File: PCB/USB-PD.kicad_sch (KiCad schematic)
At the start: 62 parts, among them J2 61300411121, Q10 SQJB90EP-T1_GE3, Q11 AO3404A, Q8 AO3404A, Q9 AO3404A, U4 TPS26750SRSMR, U5 LM2765, U6 CAT24C512YI-GT3, U7 74LVC1G08SE-7, U8 LTC7004x

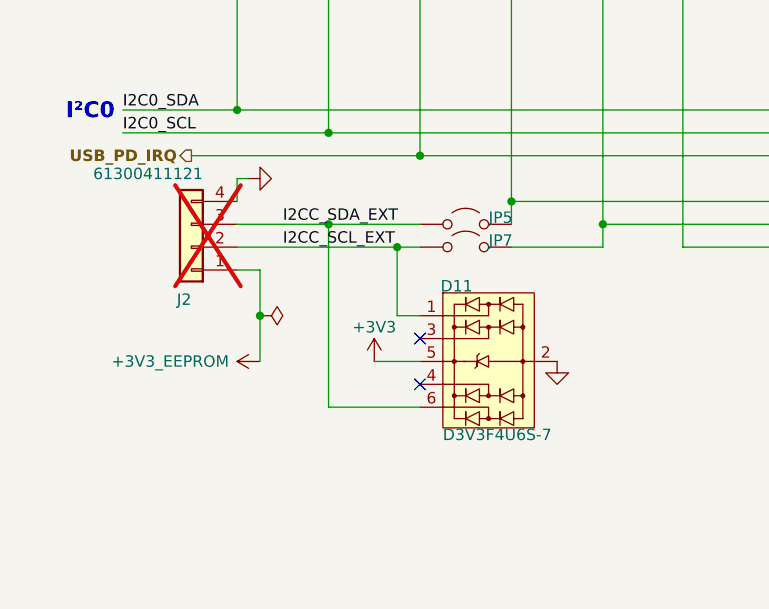
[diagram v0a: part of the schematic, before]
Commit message: Revision 2; gate diodes, 5V into LT, i2c and uart lines fixed
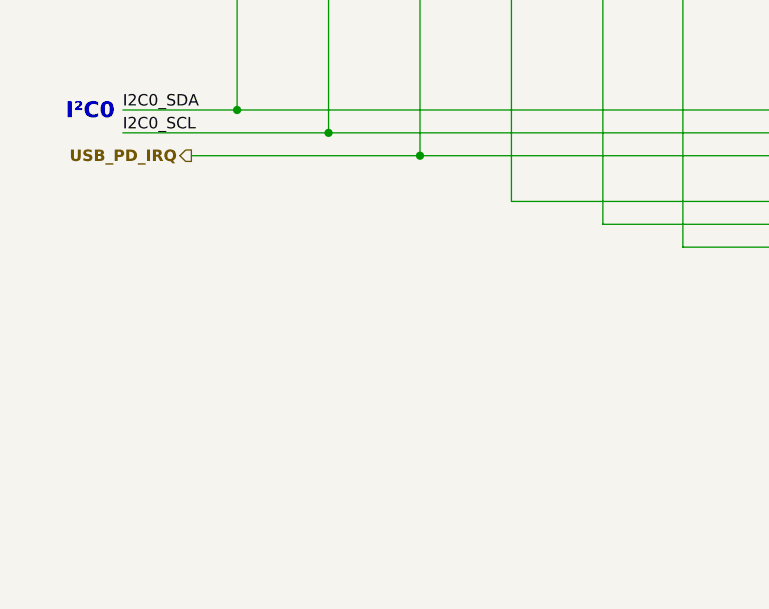
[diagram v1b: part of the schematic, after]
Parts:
- removed D11: D3V3F4U6S-7, Altium_port:sot363_sc88_65p_200x125x110_n, symbol 0_PD240W:D3V3F4U6S-7
- removed J2: 61300411121, Altium_port:we_61300411121, symbol Connector_Generic:Conn_01x04
- removed JP5, JP7: jumper_solder_2pad_no, Altium_port:jumper_solder_2pad_no_40x40_20, symbol Jumper:Jumper_2_Open
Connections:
- no-connect marks 4 -> 2

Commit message: Added NMOS output switch (rated for 20A this time)
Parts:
- removed C50: 100n X7R 100V, Capacitor_SMD:C_0603_1608Metric, symbol 0_passives:C_0603
- removed JP14: Jumper_2_Bridged, Jumper:SolderJumper-2_P1.3mm_Bridged_RoundedPad1.0x1.5mm, symbol Jumper:Jumper_2_Bridged
- removed JP4, JP6, JP8, JP9: jumper_solder_2pad_no, Jumper:SolderJumper-2_P1.3mm_Open_RoundedPad1.0x1.5mm, symbol Jumper:Jumper_2_Open
- removed R37: 100k, Resistor_SMD:R_0402_1005Metric, symbol Device:R_Small
- removed U7: 74LVC1G08SE-7, Altium_port:sot353_65p_200x125x110_mo-203-aa_n, symbol 0_PD240W:74LVC1G08SE-7
- added JP4, JP5: SolderJumper_3_Open, Jumper:SolderJumper-3_P1.3mm_Open_RoundedPad1.0x1.5mm, symbol Jumper:SolderJumper_3_Open
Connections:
- net I2CC_SCL: now also R35.2, JP4.1 (A)
- net I2CC_SCL_EEPROM: now also JP4.2 (C); no longer R35.2
- net I2CC_SCL_MCU: now also JP4.3 (B)
- net I2CC_SDA: now also R34.2, JP5.1 (A)
- net I2CC_SDA_EEPROM: now also JP5.2 (C); no longer R34.2
- net I2CC_SDA_MCU: now also JP5.3 (B)
- net PP_EN2: now also R41.1, R91.2
- net PP_EN3: no longer R41.1, R91.2
- net TS: no longer C51.1, JP11.2 (C)
- new net: C51.1, JP11.2 (C)
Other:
- moved on the sheet: Q8, Q9, R38, R39

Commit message: Preliminary finish of Rev3
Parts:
- removed D13: APTD1608LQBC/D, Altium_port:kingbright_0603_blue, symbol 0_PD240W:APTD1608LQBC/D
- removed Q11: AO3404A, Altium_port:sot-23-3L_103p_300x130x110_n, symbol Transistor_FET_Other:Q_NMOS_Depletion_GSD
- removed R45: 330R 1%, Resistor_SMD:R_0402_1005Metric, symbol 0_passives:R_0402
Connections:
- net SWITCH_EN: no longer names the net of R41.2, U8.4 (INP)

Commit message: Rev3 software now running and working. Couple hardware bugs being fixed for R4
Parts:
- removed R91: 10k, Resistor_SMD:R_0402_1005Metric, symbol Device:R
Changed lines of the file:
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@@
 	)
 	(junction
-		(at 293.37 114.3)
-		(diameter 0)
-		(color 0 0 0 0)
-	)
-	(junction
 		(at 208.28 142.24)
 		(diameter 0)
@@
 		)
 	)
-	(wire
-		(pts
-			(xy 293.37 114.3) (xy 293.37 118.11)
-		)
-		(stroke
-			(width 0)
-			(type default)
-		)
-	)
 	(bus
 		(pts
@@
 	(wire
 		(pts
-			(xy 293.37 125.73) (xy 293.37 129.54)
-		)
-		(stroke
-			(width 0)
-			(type default)
-		)
-	)
-	(wire
-		(pts
 			(xy 71.12 198.12) (xy 54.61 198.12)
 		)
@@
 	(symbol
 		(lib_id "power:GND")
-		(at 293.37 129.54 0)
-		(unit 1)
-		(body_style 1)
-		(exclude_from_sim no)
-		(in_bom yes)
-		(on_board yes)
-		(in_pos_files yes)
-		(dnp no)
-		(property "Reference" "#PWR090"
-			(at 293.37 129.54 0)
-			(hide yes)
-			(show_name no)
-			(do_not_autoplace no)
-			(effects
-				(font
-					(size 1.27 1.27)
-				)
-			)
-		)
-		(property "Value" "GND"
-			(at 293.37 135.89 0)
-			(hide yes)
-			(show_name no)
-			(do_not_autoplace no)
-			(effects
-				(font
-					(size 1.27 1.27)
-				)
-			)
-		)
-		(property "Footprint" ""
-			(at 293.37 129.54 0)
-			(show_name no)
-			(do_not_autoplace no)
-			(effects
-				(font
-					(size 1.27 1.27)
-				)
-			)
-		)
-		(property "Datasheet" ""
-			(at 293.37 129.54 0)
-			(show_name no)
-			(do_not_autoplace no)
-			(effects
-				(font
-					(size 1.27 1.27)
-				)
-			)
-		)
-		(property "Description" ""
-			(at 293.37 129.54 0)
-			(show_name no)
-			(do_not_autoplace no)
-			(effects
-				(font
-					(size 1.27 1.27)
-				)
-			)
-		)
-		(pin "1"
-		)
-		(instances
-			(project "nitride-nano"
-				(path "/aaad0350-e7db-44d5-b7ef-99e6416f6948/a05511eb-3c5e-4a0d-8491-3131eaddecdc"
-					(reference "#PWR090")
-					(unit 1)
-				)
-			)
-		)
-	)
-	(symbol
-		(lib_id "power:GND")
 		(at 143.51 74.93 0)
 		(unit 1)
@@
 					(unit 1)
 				)
-			)
-		)
-	)
-	(symbol
-		(lib_id "Device:R")
-		(at 293.37 121.92 0)
-		(mirror x)
-		(unit 1)
-		(body_style 1)
-		(exclude_from_sim no)
-		(in_bom yes)
-		(on_board yes)
-		(in_pos_files yes)
-		(dnp no)
-		(fields_autoplaced yes)
-		(property "Reference" "R91"
-			(at 295.91 123.1901 0)
-			(show_name no)
-			(do_not_autoplace no)
-			(effects
-				(font
-					(size 1.27 1.27)
-				)
-				(justify left)
-			)
-		)
-		(property "Value" "10k"
-			(at 295.91 120.6501 0)
-			(show_name no)
-			(do_not_autoplace no)
-			(effects
-				(font
-					(size 1.27 1.27)
-				)
-				(justify left)
-			)
-		)
-		(property "Footprint" "Resistor_SMD:R_0402_1005Metric"
-			(at 291.592 121.92 90)
-			(hide yes)
-			(show_name no)
-			(do_not_autoplace no)
-			(effects
-				(font
-					(size 1.27 1.27)
-				)
-			)
-		)
-		(property "Datasheet" ""
-			(at 293.37 121.92 0)
-			(hide yes)
-			(show_name no)
-			(do_not_autoplace no)
-			(effects
-				(font
-					(size 1.27 1.27)
-				)
-			)
-		)
-		(property "Description" "Resistor"
-			(at 293.37 121.92 0)
-			(hide yes)
-			(show_name no)
-			(do_not_autoplace no)
-			(effects
-				(font
-					(size 1.27 1.27)
-				)
-			)
-		)
-		(property "LCSC" "C2906861"
-			(at 295.91 123.1901 0)
-			(hide yes)
-			(show_name no)
-			(do_not_autoplace no)
-			(effects
-				(font
-					(size 1.27 1.27)
-				)
-			)
-		)
-		(pin "2"
-		)
-		(pin "1"
-		)
-		(instances
-			(project "nitride-nano"
-				(path "/aaad0350-e7db-44d5-b7ef-99e6416f6948/a05511eb-3c5e-4a0d-8491-3131eaddecdc"
-					(reference "R91")
-					(unit 1)
-				)
